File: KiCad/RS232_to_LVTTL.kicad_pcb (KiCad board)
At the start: 2 copper layers, 36.1 x 34 mm, 10 parts, among them J1 DB25_Female, U1 TPS54308, U2 MAX3232

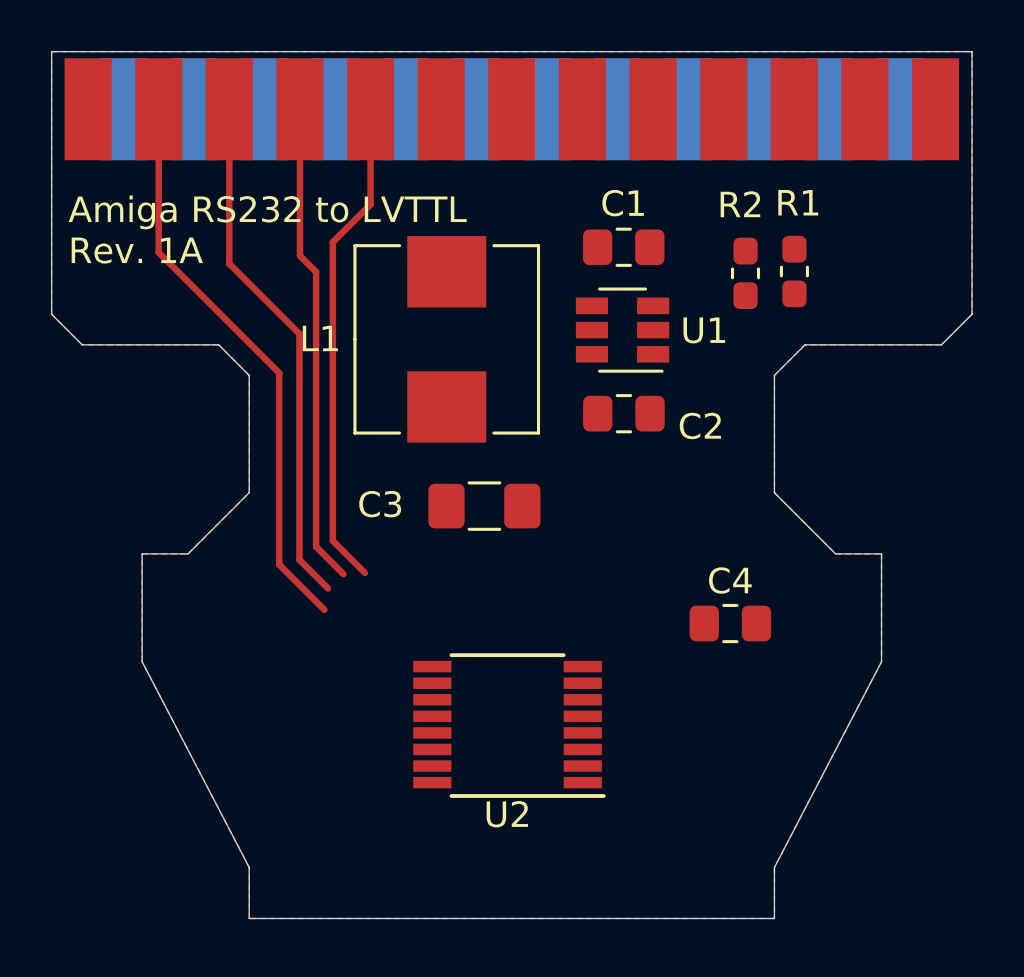
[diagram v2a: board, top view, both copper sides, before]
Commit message: Added 5-pin header for TX,RX,RTS,CTS,GND
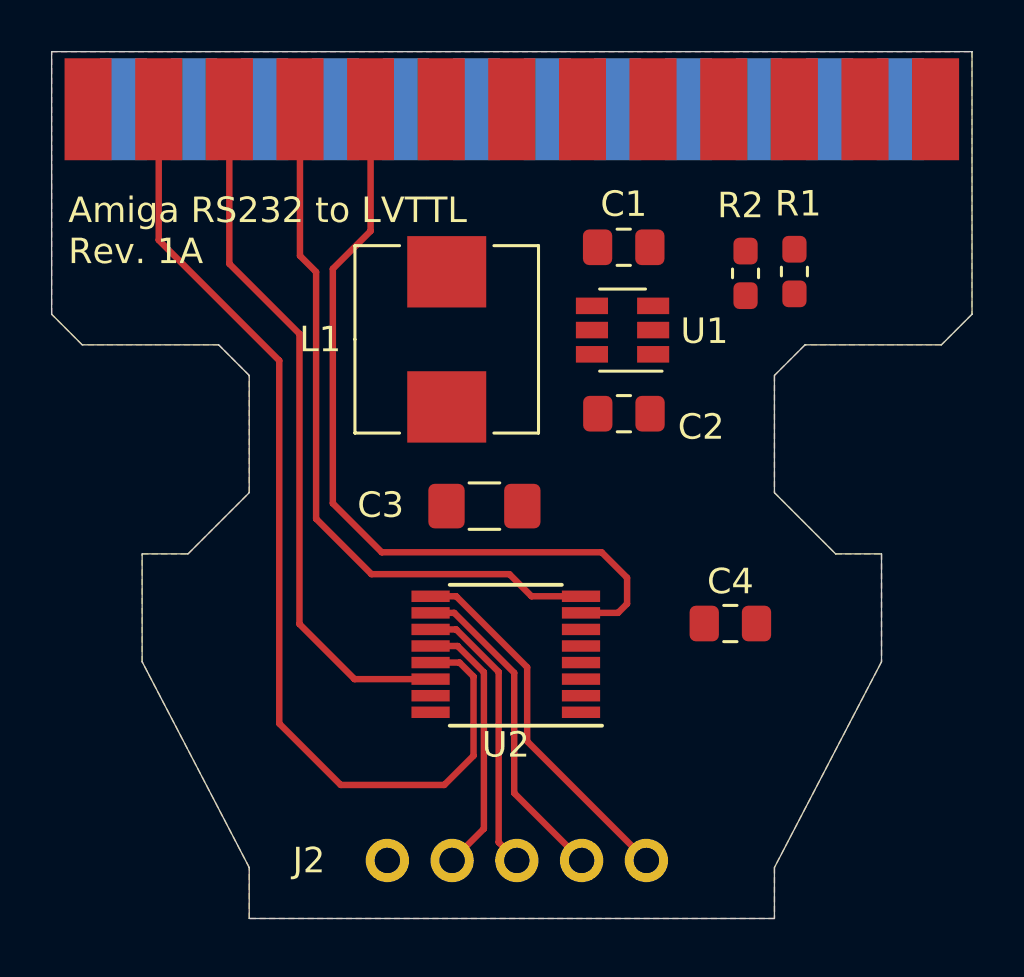
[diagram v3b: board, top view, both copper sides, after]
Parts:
- added J2: Conn_01x05, Connector_PinHeader_2.54mm:PinHeader_1x05_P2.54mm_Vertical, F.Cu at (101.6, 81.7)
- moved U2 2.76 mm to (106.3, 73.6)
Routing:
- net TX: track 22.6 -> 40.4 mm
- net CTS_MCU: track 0.00 -> 14.5 mm
- net RTS_MCU: track 0.00 -> 12.7 mm
- net CTS: track 19.6 -> 32.1 mm
- net TX_MCU: track 0.00 -> 11.1 mm
- net RX_MCU: track 0.00 -> 10.4 mm
- net RTS: track 19.2 -> 28.2 mm
- net RX: track 20.7 -> 27.6 mm
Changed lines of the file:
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@@
     (thickness 1.6)
     (drawings 24)
-    (tracks 16)
+    (tracks 46)
     (zones 0)
-    (modules 10)
+    (modules 11)
     (nets 41)
   )
@@
   )
   (setup
-    (last_trace_width 0.2032)
+    (last_trace_width 0.254)
     (user_trace_width 0.1524)
     (user_trace_width 0.1778)
@@
     (add_net TX_MCU)
   )
+  (module Connector_PinHeader_2.54mm:PinHeader_1x05_P2.54mm_Vertical (layer F.Cu)
+    (at 101.61736 81.7246 90)
+    (descr "Through hole straight pin header, 1x05, 2.54mm pitch, single row")
+    (tags "Through hole pin header THT 1x05 2.54mm single row")
+    (fp_text reference J2 (at 0 -3.07594 180) (layer F.SilkS)
+      (effects (font (size 1 1) (thickness 0.15)))
+    )
+    (fp_text value Conn_01x05 (at 0 12.49 90) (layer F.Fab) hide
+      (effects (font (size 1 1) (thickness 0.15)))
+    )
+    (fp_line (start 1.8 -1.8) (end -1.8 -1.8) (layer F.CrtYd) (width 0.05))
+    (fp_line (start 1.8 11.95) (end 1.8 -1.8) (layer F.CrtYd) (width 0.05))
+    (fp_line (start -1.8 11.95) (end 1.8 11.95) (layer F.CrtYd) (width 0.05))
+    (fp_line (start -1.8 -1.8) (end -1.8 11.95) (layer F.CrtYd) (width 0.05))
+    (fp_line (start -1.27 -0.635) (end -0.635 -1.27) (layer F.Fab) (width 0.1))
+    (fp_line (start -1.27 11.43) (end -1.27 -0.635) (layer F.Fab) (width 0.1))
+    (fp_line (start 1.27 11.43) (end -1.27 11.43) (layer F.Fab) (width 0.1))
+    (fp_line (start 1.27 -1.27) (end 1.27 11.43) (layer F.Fab) (width 0.1))
+    (fp_line (start -0.635 -1.27) (end 1.27 -1.27) (layer F.Fab) (width 0.1))
+    (fp_text user %R (at 0 5.08) (layer F.Fab) hide
+      (effects (font (size 1 1) (thickness 0.15)))
+    )
+    (pad 5 thru_hole oval (at 0 10.16 90) (size 1.7 1.7) (drill 1) (layers *.Cu *.Mask)
+      (net 40 CTS_MCU))
+    (pad 4 thru_hole oval (at 0 7.62 90) (size 1.7 1.7) (drill 1) (layers *.Cu *.Mask)
+      (net 39 RTS_MCU))
+    (pad 3 thru_hole oval (at 0 5.08 90) (size 1.7 1.7) (drill 1) (layers *.Cu *.Mask)
+      (net 38 TX_MCU))
+    (pad 2 thru_hole oval (at 0 2.54 90) (size 1.7 1.7) (drill 1) (layers *.Cu *.Mask)
+      (net 37 RX_MCU))
+    (pad 1 thru_hole oval (at 0 0 90) (size 1.7 1.7) (drill 1) (layers *.Cu *.Mask)
+      (net 1 GND))
+  )
   (module Package_SO:TSSOP-16_4.4x5mm_P0.65mm (layer F.Cu)
-    (at 106.3316 76.39568 180)
+    (at 106.26302 73.63724 180)
     (descr "16-Lead Plastic Thin Shrink Small Outline (ST)-4.4 mm Body [TSSOP] (see Microchip Packaging Specification 00000049BS.pdf)")
     (tags "SSOP 0.65")
@@
   (gr_line (start 124.55 50) (end 124.55 60.3) (layer Edge.Cuts) (width 0.05))
   (gr_line (start 88.45 50) (end 124.55 50) (layer Edge.Cuts) (width 0.05))
-  (segment (start 100.96 52) (end 100.96 55.9939) (width 0.254) (layer F.Cu) (net 26))
-  (segment (start 100.96 55.9939) (end 99.47868 57.47522) (width 0.254) (layer F.Cu) (net 26))
-  (segment (start 99.47868 57.47522) (end 99.47868 69.18716) (width 0.254) (layer F.Cu) (net 26))
-  (segment (start 99.47868 69.18716) (end 100.73852 70.447) (width 0.254) (layer F.Cu) (net 26))
+  (segment (start 110.02222 69.63674) (end 111.02044 70.63496) (width 0.254) (layer F.Cu) (net 26))
+  (segment (start 111.02044 71.65604) (end 110.66424 72.01224) (width 0.254) (layer F.Cu) (net 26))
+  (segment (start 101.39892 69.63674) (end 110.02222 69.63674) (width 0.254) (layer F.Cu) (net 26))
+  (segment (start 111.02044 70.63496) (end 111.02044 71.65604) (width 0.254) (layer F.Cu) (net 26))
+  (segment (start 99.47868 67.7165) (end 101.39892 69.63674) (width 0.254) (layer F.Cu) (net 26))
+  (segment (start 110.66424 72.01224) (end 109.21302 72.01224) (width 0.254) (layer F.Cu) (net 26))
+  (segment (start 99.47868 58.51916) (end 99.47868 67.7165) (width 0.254) (layer F.Cu) (net 26))
+  (segment (start 100.96 57.03784) (end 99.47868 58.51916) (width 0.254) (layer F.Cu) (net 26))
+  (segment (start 100.96 52) (end 100.96 57.03784) (width 0.254) (layer F.Cu) (net 26))
+  (segment (start 107.27224 71.36224) (end 109.21302 71.36224) (width 0.254) (layer F.Cu) (net 27))
+  (segment (start 106.40526 70.49526) (end 107.27224 71.36224) (width 0.254) (layer F.Cu) (net 27))
+  (segment (start 100.99506 70.49526) (end 106.40526 70.49526) (width 0.254) (layer F.Cu) (net 27))
+  (segment (start 98.82336 68.32356) (end 100.99506 70.49526) (width 0.254) (layer F.Cu) (net 27))
+  (segment (start 98.82336 58.64108) (end 98.82336 68.32356) (width 0.254) (layer F.Cu) (net 27))
+  (segment (start 98.19 58.00772) (end 98.82336 58.64108) (width 0.254) (layer F.Cu) (net 27))
   (segment (start 98.19 52) (end 98.19 58.00772) (width 0.254) (layer F.Cu) (net 27))
-  (segment (start 98.19 58.00772) (end 98.82336 58.64108) (width 0.254) (layer F.Cu) (net 27))
-  (segment (start 98.82336 58.64108) (end 98.82336 69.42084) (width 0.254) (layer F.Cu) (net 27))
-  (segment (start 98.82336 69.42084) (end 99.89778 70.49526) (width 0.254) (layer F.Cu) (net 27))
-  (segment (start 95.42 52) (end 95.42 58.31874) (width 0.254) (layer F.Cu) (net 35))
-  (segment (start 95.42 58.31874) (end 98.17058 61.06932) (width 0.254) (layer F.Cu) (net 35))
-  (segment (start 98.17058 61.06932) (end 98.17058 69.93392) (width 0.254) (layer F.Cu) (net 35))
-  (segment (start 98.17058 69.93392) (end 99.29072 71.05406) (width 0.254) (layer F.Cu) (net 35))
-  (segment (start 92.65 52) (end 92.65 57.88046) (width 0.254) (layer F.Cu) (net 36))
-  (segment (start 92.65 57.88046) (end 97.3781 62.60856) (width 0.254) (layer F.Cu) (net 36))
-  (segment (start 97.3781 62.60856) (end 97.3781 70.12188) (width 0.254) (layer F.Cu) (net 36))
-  (segment (start 97.3781 70.12188) (end 99.15102 71.8948) (width 0.254) (layer F.Cu) (net 36))
+  (segment (start 98.17058 61.06932) (end 95.42 58.31874) (width 0.254) (layer F.Cu) (net 35))
+  (segment (start 95.42 58.31874) (end 95.42 52) (width 0.254) (layer F.Cu) (net 35))
+  (segment (start 98.17058 72.45106) (end 98.17058 61.06932) (width 0.254) (layer F.Cu) (net 35))
+  (segment (start 100.33176 74.61224) (end 98.17058 72.45106) (width 0.254) (layer F.Cu) (net 35))
+  (segment (start 103.31302 74.61224) (end 100.33176 74.61224) (width 0.254) (layer F.Cu) (net 35))
+  (segment (start 104.44934 73.96224) (end 103.31302 73.96224) (width 0.254) (layer F.Cu) (net 36))
+  (segment (start 104.9981 77.61488) (end 104.9981 74.511) (width 0.254) (layer F.Cu) (net 36))
+  (segment (start 99.78856 78.76296) (end 103.85002 78.76296) (width 0.254) (layer F.Cu) (net 36))
+  (segment (start 104.9981 74.511) (end 104.44934 73.96224) (width 0.254) (layer F.Cu) (net 36))
+  (segment (start 103.85002 78.76296) (end 104.9981 77.61488) (width 0.254) (layer F.Cu) (net 36))
+  (segment (start 97.3781 76.3525) (end 99.78856 78.76296) (width 0.254) (layer F.Cu) (net 36))
+  (segment (start 92.65 57.39024) (end 97.3781 62.11834) (width 0.254) (layer F.Cu) (net 36))
+  (segment (start 97.3781 62.11834) (end 97.3781 76.3525) (width 0.254) (layer F.Cu) (net 36))
+  (segment (start 92.65 52) (end 92.65 57.39024) (width 0.254) (layer F.Cu) (net 36))
+  (segment (start 105.40451 74.34266) (end 105.40451 80.47745) (width 0.254) (layer F.Cu) (net 37))
+  (segment (start 104.37409 73.31224) (end 105.40451 74.34266) (width 0.254) (layer F.Cu) (net 37))
+  (segment (start 105.40451 80.47745) (end 104.15736 81.7246) (width 0.254) (layer F.Cu) (net 37))
+  (segment (start 103.31302 73.31224) (end 104.37409 73.31224) (width 0.254) (layer F.Cu) (net 37))
+  (segment (start 104.31702 72.66224) (end 105.98362 74.32884) (width 0.254) (layer F.Cu) (net 38))
+  (segment (start 103.31302 72.66224) (end 104.31702 72.66224) (width 0.254) (layer F.Cu) (net 38))
+  (segment (start 105.98362 81.01086) (end 106.69736 81.7246) (width 0.254) (layer F.Cu) (net 38))
+  (segment (start 105.98362 74.32884) (end 105.98362 81.01086) (width 0.254) (layer F.Cu) (net 38))
+  (segment (start 104.24177 72.01224) (end 106.59322 74.36369) (width 0.254) (layer F.Cu) (net 39))
+  (segment (start 103.31302 72.01224) (end 104.24177 72.01224) (width 0.254) (layer F.Cu) (net 39))
+  (segment (start 106.59322 79.08046) (end 109.23736 81.7246) (width 0.254) (layer F.Cu) (net 39))
+  (segment (start 106.59322 74.36369) (end 106.59322 79.08046) (width 0.254) (layer F.Cu) (net 39))
+  (segment (start 104.31702 71.36224) (end 107.10122 74.14644) (width 0.254) (layer F.Cu) (net 40))
+  (segment (start 103.31302 71.36224) (end 104.31702 71.36224) (width 0.254) (layer F.Cu) (net 40))
+  (segment (start 107.10122 77.04846) (end 111.77736 81.7246) (width 0.254) (layer F.Cu) (net 40))
+  (segment (start 107.10122 74.14644) (end 107.10122 77.04846) (width 0.254) (layer F.Cu) (net 40))
   (zone (net 1) (net_name GND) (layer B.Cu) (hatch edge 0.508)
     (connect_pads (clearance 0.1524))

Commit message: Fixed positioning of 5-pin header
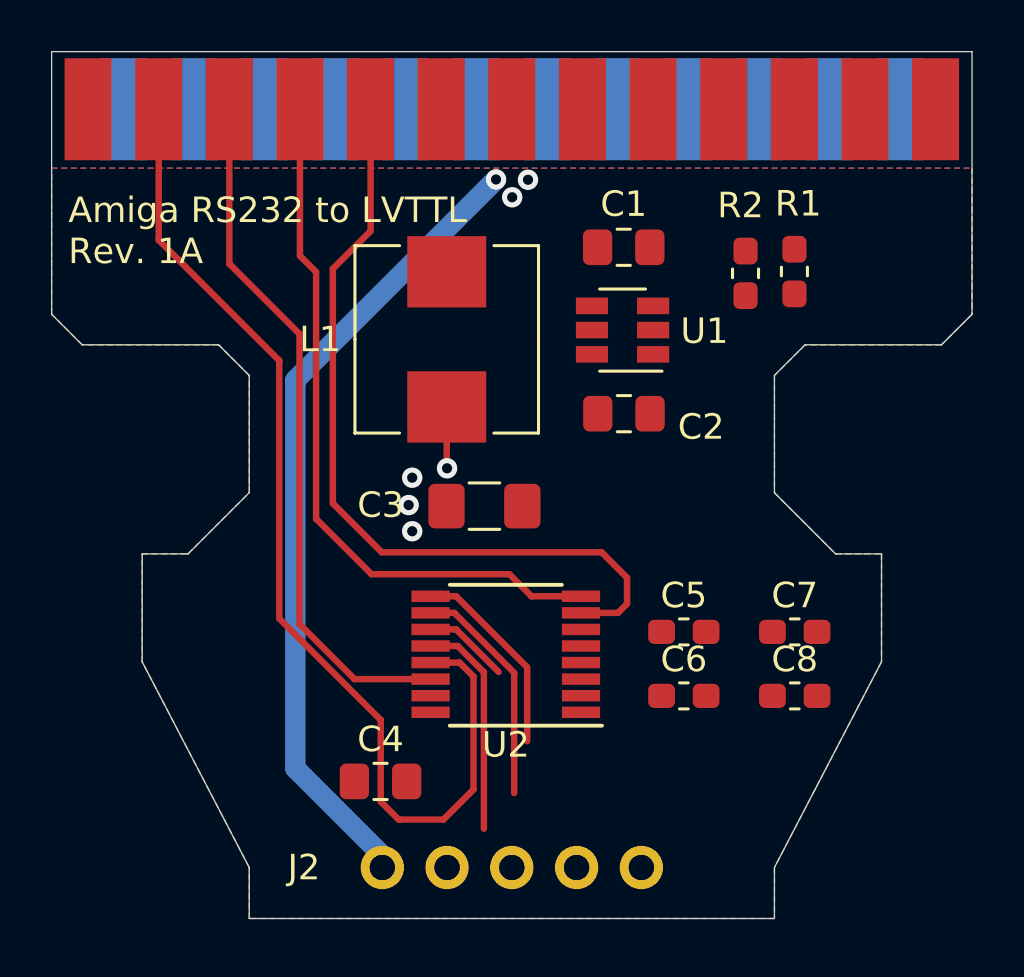
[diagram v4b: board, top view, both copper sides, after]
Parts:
- added C5: 100nF, Capacitor_SMD:C_0603_1608Metric_Pad1.05x0.95mm_HandSolder, F.Cu at (113.2, 72.8)
- added C6: 100nF, Capacitor_SMD:C_0603_1608Metric_Pad1.05x0.95mm_HandSolder, F.Cu at (113.2, 75.3)
- added C7: 100nF, Capacitor_SMD:C_0603_1608Metric_Pad1.05x0.95mm_HandSolder, F.Cu at (117.6, 72.8)
- added C8: 100nF, Capacitor_SMD:C_0603_1608Metric_Pad1.05x0.95mm_HandSolder, F.Cu at (117.6, 75.3)
- moved C4 15.1 mm to (101.4, 78.6)
- moved J2 0.34 mm to (101.4, 82.0)
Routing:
- net GND: track 0.00 -> 31.5 mm, vias 0 -> 3
- net TX_MCU: track 11.1 -> 3.36 mm
- net CTS_MCU: track 14.5 -> 7.84 mm
- net RTS_MCU: track 12.7 -> 8.97 mm
- net 3V3: track 0.00 -> 2.41 mm, vias 0 -> 4
- net RX_MCU: track 10.4 -> 8.65 mm
- net TX: track 40.4 -> 41.8 mm
- added copper zone on B.Cu, net 3V3
- removed copper zone on B.Cu, net GND

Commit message: routing and placing of components
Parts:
- removed the C6 at (113.2, 75.3)
- added C7: 100nF, Capacitor_SMD:C_0603_1608Metric_Pad1.05x0.95mm_HandSolder, F.Cu at (114.3, 72.9)
- added D1: LED, Diode_SMD:D_0603_1608Metric_Pad1.05x0.95mm_HandSolder, F.Cu at (104.0, 78.4)
- added D2: LED, Diode_SMD:D_0603_1608Metric_Pad1.05x0.95mm_HandSolder, F.Cu at (105.7, 78.4)
- added R3: 1k, Resistor_SMD:R_0603_1608Metric_Pad1.05x0.95mm_HandSolder, F.Cu at (98.7, 77.4)
- added R4: 1k, Resistor_SMD:R_0603_1608Metric_Pad1.05x0.95mm_HandSolder, F.Cu at (98.7, 79.0)
- moved C2 11.1 mm to (119.8, 57.6), turned to 180 degrees
- moved R1 9.26 mm to (112.9, 66.6)
- moved R2 9.07 mm to (111.2, 66.6)
- moved C8 5.20 mm to (114.3, 71.2)
- moved C4 5.02 mm to (99.4, 74.0), turned to 90 degrees
- moved C6 3.75 mm to (114.3, 74.5)
- moved C5 3.60 mm to (114.3, 76.2)
- moved U1 2.27 mm to (113.0, 61.6), turned to 270 degrees
- moved C1 2.11 mm to (113.0, 57.6), turned to 0 degrees
- moved U2 0.59 mm to (106.5, 73.1)
- moved L1 0.36 mm to (104.0, 60.9)
- moved C3 0.33 mm to (105.4, 67.5)
- renumbered C7 to C6
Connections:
- C4 pad 1: GND -> 3V3
- C4 pad 2: 3V3 -> GND
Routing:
- net GND: track 31.5 -> 91.4 mm, vias 3 -> 9
- net 3V3: track 2.41 -> 41.1 mm, vias 4 -> 11
- net Net-(C2-Pad2): track 0.00 -> 21.0 mm
- net TX_MCU: track 3.36 -> 13.5 mm
- net Net-(C2-Pad1): track 0.00 -> 9.56 mm
- net 12V: track 0.00 -> 8.58 mm
- net Net-(C5-Pad1): track 0.00 -> 8.24 mm
- net CTS_MCU: track 7.84 -> 15.4 mm
- net Net-(D2-Pad2): track 0.00 -> 6.76 mm
- net Net-(R1-Pad1): track 0.00 -> 6.61 mm
- net Net-(C7-Pad1): track 0.00 -> 6.36 mm
- net Net-(C5-Pad2): track 0.00 -> 6.07 mm
- net RX_MCU: track 8.65 -> 13.5 mm
- net RTS_MCU: track 8.97 -> 13.8 mm
- net Net-(D1-Pad2): track 0.00 -> 4.44 mm
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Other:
- board text added: "CTS"
- board text added: "GND"
- board text added: "RS232 to LVTTL Amiga version Rev. 1A"
- board text added: "RTS"
- board text added: "RX"
- board text added: "TX"
- board text removed: "Amiga RS232 to LVTTL Rev. 1A"
